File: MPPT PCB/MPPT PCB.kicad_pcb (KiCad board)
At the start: 2 copper layers, 62.2 x 78.1 mm, 29 parts, among them J1 Conn_01x03_Male, J10 Conn_01x03_Male, J11 Conn_01x03_Male, J12 Conn_01x03_Male, J13 Conn_01x03_Male, J2 Conn_01x03_Male, J3 Conn_01x06_Female, J4 Conn_01x03_Male, J5 Screw_Terminal_01x02, J6 Conn_01x03_Male, J7 Conn_01x03_Male, J8 Screw_Terminal_01x02, J9 Conn_01x06_Female, P1 Conn_01x15_Female, P2 Conn_01x15_Female, SW1 SW_Push

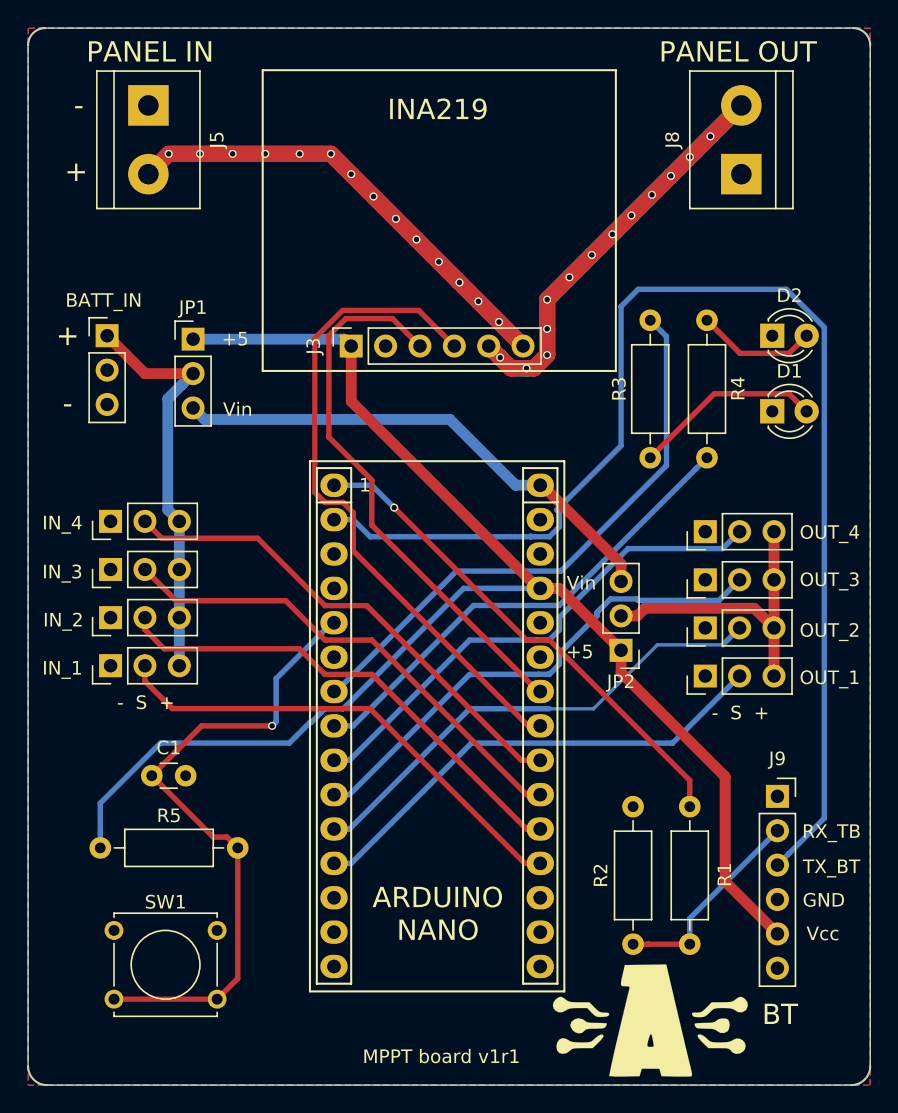
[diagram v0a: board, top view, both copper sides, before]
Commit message: Fixed servo pinout (Input and Output)
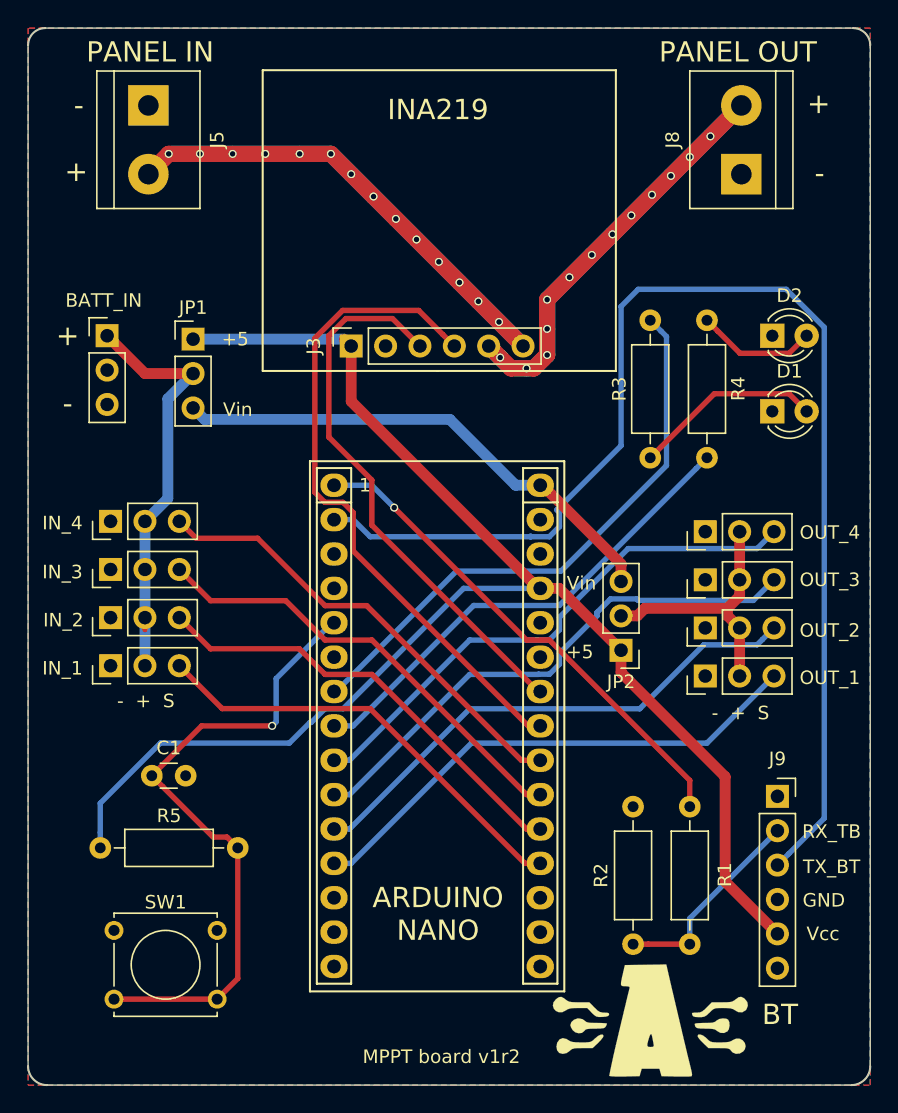
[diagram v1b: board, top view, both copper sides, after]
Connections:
- J1 pad 2: PPM_IN_1 -> PWR_IN
- J1 pad 3: PWR_IN -> PPM_IN_1
- J10 pad 2: PPM_OUT_1 -> PWR_OUT
- J10 pad 3: PWR_OUT -> PPM_OUT_1
- J11 pad 2: PPM_OUT_3 -> PWR_OUT
- J11 pad 3: PWR_OUT -> PPM_OUT_3
- J12 pad 2: PPM_OUT_4 -> PWR_OUT
- J12 pad 3: PWR_OUT -> PPM_OUT_4
- J13 pad 2: PPM_OUT_2 -> PWR_OUT
- J13 pad 3: PWR_OUT -> PPM_OUT_2
- J2 pad 2: PPM_IN_3 -> PWR_IN
- J2 pad 3: PWR_IN -> PPM_IN_3
- J6 pad 2: PPM_IN_2 -> PWR_IN
- J6 pad 3: PWR_IN -> PPM_IN_2
- J7 pad 2: PPM_IN_4 -> PWR_IN
- J7 pad 3: PWR_IN -> PPM_IN_4
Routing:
- net PWR_OUT: track 22.8 -> 19.5 mm
- net PPM_IN_1: track 35.9 -> 32.7 mm
- net PPM_IN_2: track 36.2 -> 33.1 mm
- net PPM_OUT_3: track 37.3 -> 39.8 mm
- net PPM_OUT_2: track 36.1 -> 38.7 mm
- net PPM_OUT_1: track 35.7 -> 38.2 mm
- net PPM_IN_3: track 36.1 -> 33.6 mm
- net PPM_OUT_4: track 37.5 -> 40.0 mm
- net PPM_IN_4: track 36.5 -> 34.0 mm
- net PWR_IN: track 30.2 -> 31.5 mm
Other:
- board text added: "- + S"
- board text added: "MPPT board v1r2"
- board text removed: "- S +"
- board text removed: "MPPT board v1r1"

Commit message: Version 2 of PCB
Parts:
- removed the G*** at (146.2, 49.5)
- added J14: Conn_01x01_Male, digikey-footprints:Test_Point_2.67x1.02mm, B.Cu at (146.1, 39.4)
- added J15: Conn_01x01_Male, digikey-footprints:Test_Point_2.67x1.02mm, B.Cu at (151.1, 39.4)
- added J16: Conn_01x01_Male, digikey-footprints:Test_Point_2.67x1.02mm, B.Cu at (148.6, 39.4)
- added J17: Conn_01x01_Male, digikey-footprints:Test_Point_2.67x1.02mm, B.Cu at (143.5, 39.4)
- added REF**: MountingHole_2.2mm_M2, MountingHole:MountingHole_2.2mm_M2, F.Cu at (176.5, 40.0)
- added REF**: MountingHole_2.2mm_M2, MountingHole:MountingHole_2.2mm_M2, F.Cu at (119.4, 40.0)
- added REF**: MountingHole_2.2mm_M2, MountingHole:MountingHole_2.2mm_M2, F.Cu at (176.5, 113.0)
- added REF**: MountingHole_2.2mm_M2, MountingHole:MountingHole_2.2mm_M2, F.Cu at (119.4, 113.0)
- D1: value LED -> LED_G
- D2: value LED -> LED_O
- G***: value LOGO -> (none); moved to B.Cu
- R3, R4: value 1K -> 150R
- moved G*** 16.2 mm to (147.1, 110.2), turned to 180 degrees
- moved J8 2.79 mm to (169.5, 51.1)
- moved J5 2.79 mm to (125.7, 46.0)
- moved J4 0.25 mm to (122.7, 60.5)
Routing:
- net SDA: track 49.1 -> 119.5 mm
- net SCL: track 41.0 -> 107.4 mm
- net +5V: track 112.4 -> 161.5 mm
- net PANEL_IN: track 66.3 -> 63.6 mm
- net PANEL_OUT: track 59.6 -> 57.3 mm
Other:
- outline, holes or cut-outs redrawn
- board text added: "+5V"
- board text added: "Engineered in the rainy Galicia"
- board text added: "IN"
- board text added: "MPPT board v2r0"
- board text added: "OUT"
- board text added: "RX_BT"
- board text added: "SC ROBOTICS"
- board text added: "SCL"
- board text added: "SDA"
- board text added: "www.scrobotics.es"
- board text removed: "Diseñado por: Luis Miranda Hernán Serrano"
- board text removed: "MPPT board v1r2"
- board text removed: "PANEL IN"
- board text removed: "PANEL OUT"
- board text removed: "RX_TB"
